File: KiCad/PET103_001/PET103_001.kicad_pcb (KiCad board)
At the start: 2 copper layers, 44 parts, among them J1 B1 GND, J10 P, J11 V, J12 LA4140, J2 B2 GND, J3 B3 GND, J4 B4 GND, J5 R VCC, J6 W, J7 O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

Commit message: Updated schematics and PCB with new symbols and rearranged the layout. Added one more datasheet and KiCad symbol for LA4140.
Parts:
- removed J12: LA4140, Connector_PinHeader_2.54mm:PinHeader_1x09_P2.54mm_Vertical
- added U2: LA4140, Package_SIP:SIP9_Housing_BigPads, F.Cu at (166.8, 74.9)
- J1: value B1 GND -> Battery GND
- J10: value P -> Keyboard 2
- J11: value V -> Vibrate Switch
- J2: value B2 GND -> Speaker GND
- J3: value B3 GND -> Slider GND
- J4: value B4 GND -> Vibrate GND
- J5: value R VCC -> VCC on/off
- J6: value W -> Speaker +
- J7: value O -> Slider 1
- J8: value G -> Slider 2
- J9: value Y -> Keyboard 1
- moved C7 2.86 mm to (167.0, 103.8), turned to 225 degrees
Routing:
- net Net-(C7-Pad1): track 22.1 -> 20.0 mm

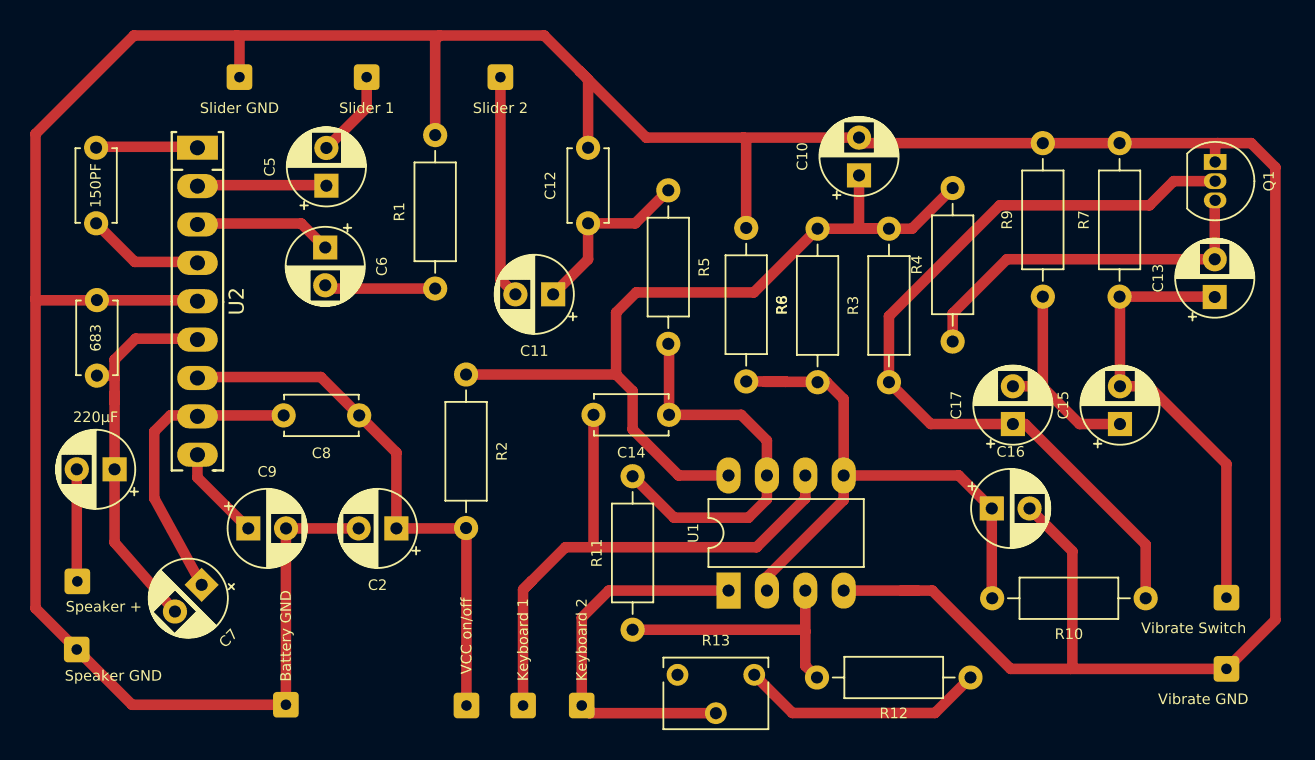
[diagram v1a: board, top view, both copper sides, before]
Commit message: Print for keyboard PCB
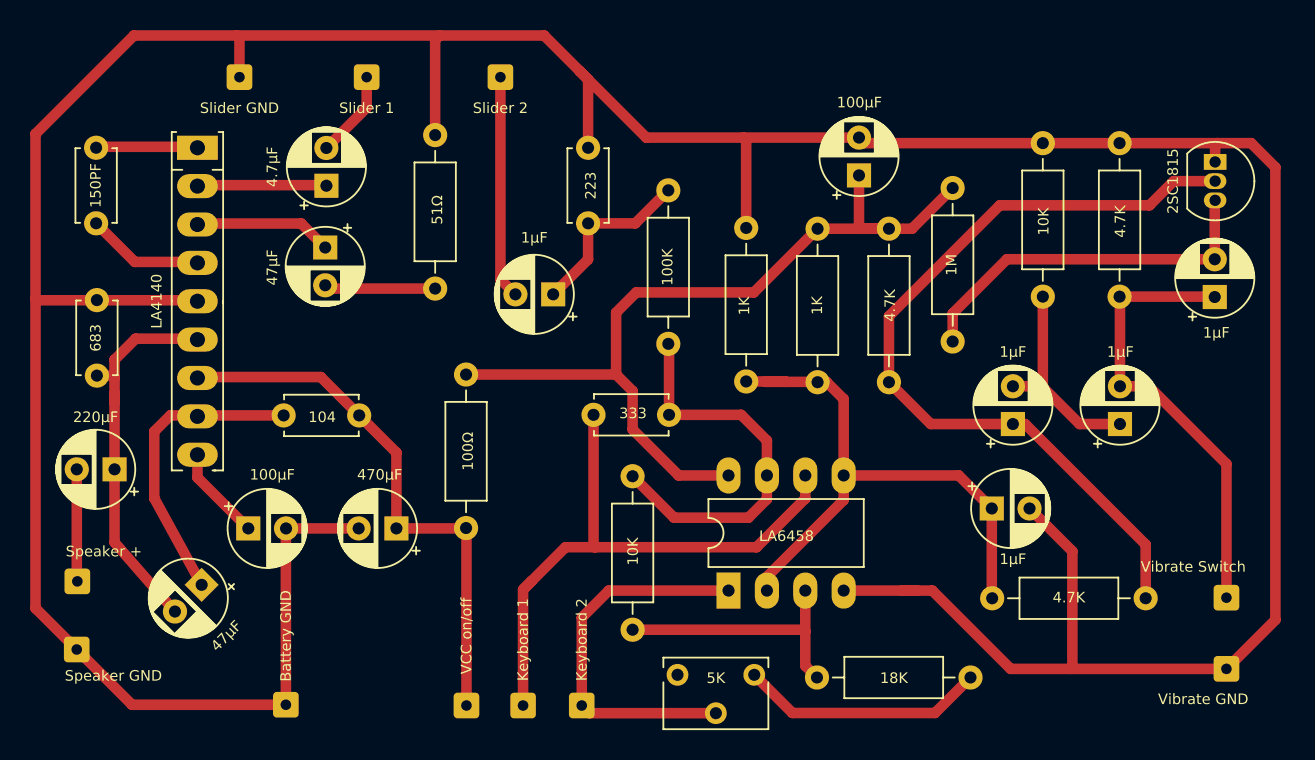
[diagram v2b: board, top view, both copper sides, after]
